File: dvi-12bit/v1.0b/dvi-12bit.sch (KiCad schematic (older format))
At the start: 33 parts, among them J1 PMOD, J2 PMOD, J3 jmp, J4 5V, J6 HDMI_A_1.4, U1 VREG_3V3, U2 TFP410

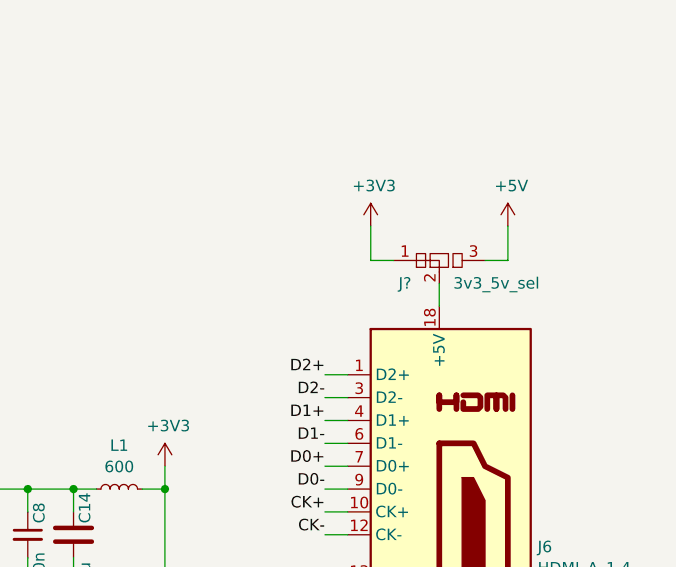
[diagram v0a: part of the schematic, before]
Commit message: A few minor fixes to the dvi PMODs.
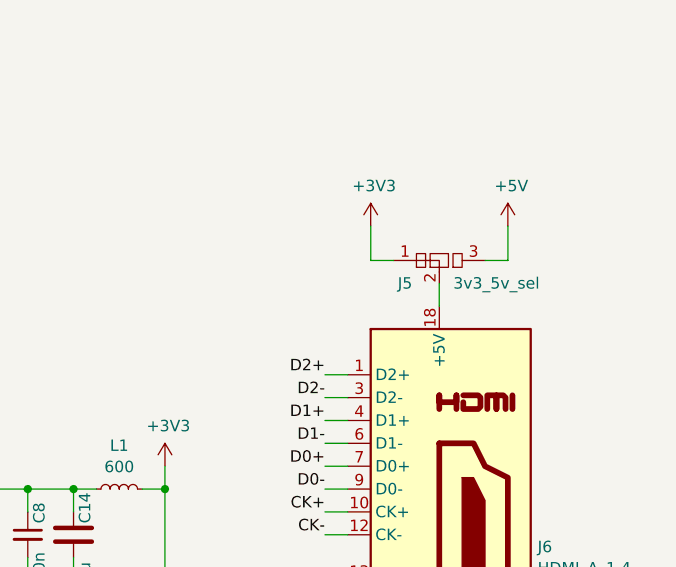
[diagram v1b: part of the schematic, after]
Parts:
- gave numbers to parts that had none: 1
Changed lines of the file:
@@
 B0
 $Comp
-L pkl_misc:pkl_double_jumper_ncno J?
+L pkl_misc:pkl_double_jumper_ncno J5
 U 1 1 5C5DF288
 P 9400 2400
-F 0 "J?" H 9250 2500 50  0000 C CNN
+F 0 "J5" H 9250 2500 50  0000 C CNN
 F 1 "3v3_5v_sel" H 9650 2500 50  0000 C CNN
 F 2 "pkl_jumpers:J_NCNO_0903_30" H 9350 2400 50  0001 C CNN
@@
 	9700 2400 9700 2250
 $Comp
-L power:+3V3 #PWR?
+L power:+3V3 #PWR0128
 U 1 1 5C5F0282
 P 9100 2250
-F 0 "#PWR?" H 9100 2100 50  0001 C CNN
+F 0 "#PWR0128" H 9100 2100 50  0001 C CNN
 F 1 "+3V3" H 9115 2426 50  0000 C CNN
 F 2 "" H 9100 2250 50  0001 C CNN
